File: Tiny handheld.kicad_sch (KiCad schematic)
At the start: 38 parts, among them J1 Conn_01x04_Female, J2 Conn_01x04_Female, J3 TYPE-C-31-M-12, U1 ATtiny85-20P, U2 ATtiny85-20M, U3 EEPROM-I2CEIAJ

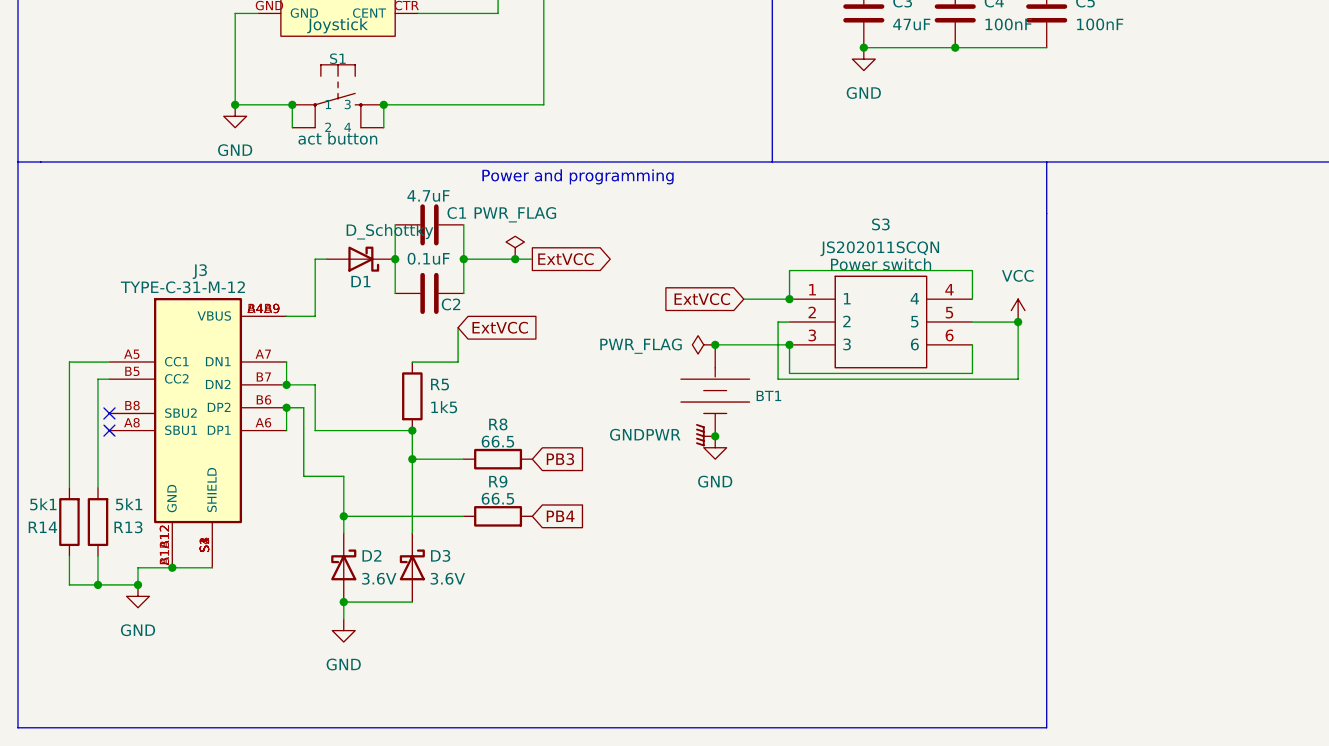
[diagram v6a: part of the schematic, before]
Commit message: added different switch in schematic
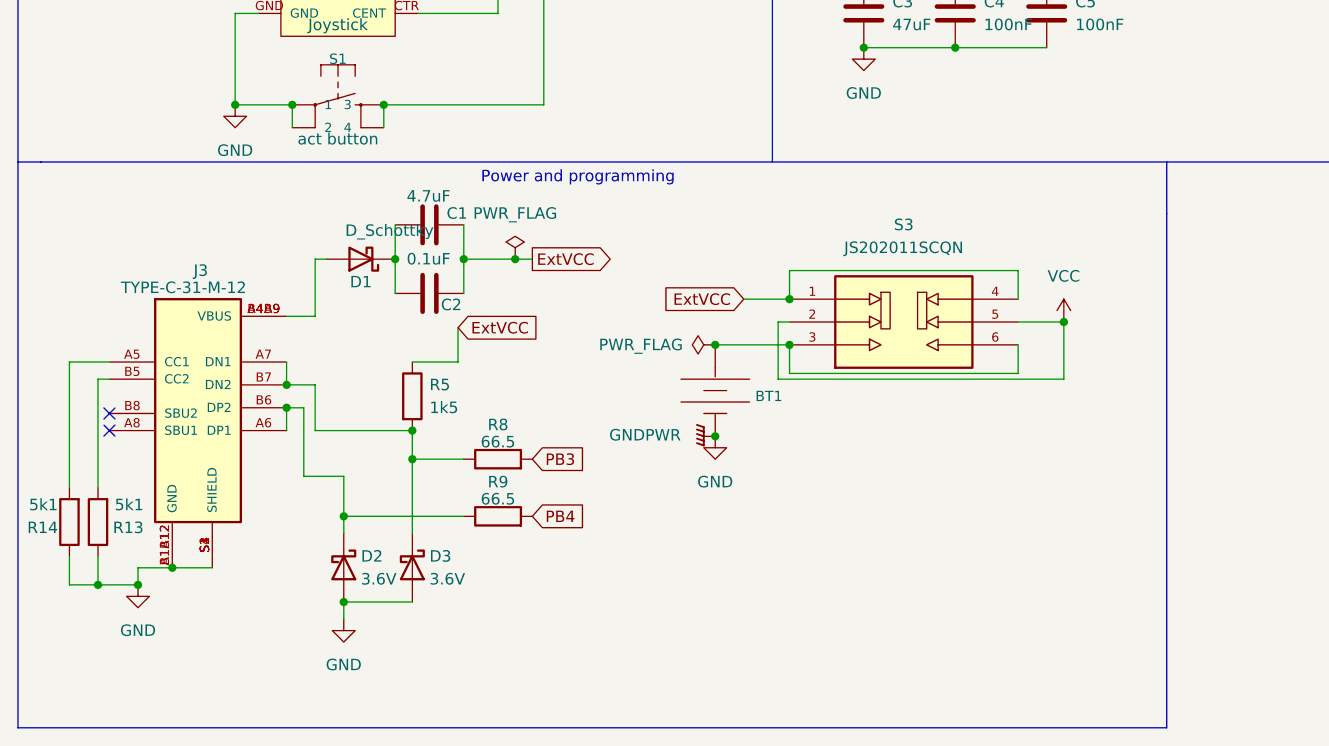
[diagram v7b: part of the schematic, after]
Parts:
- removed S3: JS202011SCQN, SmacSYs:JS202011SCQN, symbol SamacSys_Parts:JS202011SCQN
- added S3: JS202011SCQN, SnapEDA Library:SW_JS202011SCQN, symbol JS202011SCQN:JS202011SCQN
- U3: footprint Package_SO:SOIC-8-1EP_3.9x4.9mm_P1.27mm_EP2.41x3.81mm -> Package_SO:SOIC-8_3.9x4.9mm_P1.27mm
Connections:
- net ExtVCC: now also S3.1, S3.4
- net VCC: now also S3.2, S3.5
- net at BT1.+: now also S3.3, S3.6
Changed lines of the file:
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@@
   (junction (at 249.555 27.305) (diameter 0) (color 0 0 0 0)
   )
+  (junction (at 248.285 29.845) (diameter 0) (color 0 0 0 0)
+  )
+  (junction (at 132.715 54.61) (diameter 0) (color 0 0 0 0)
+  )
+  (junction (at 71.12 45.085) (diameter 0) (color 0 0 0 0)
+  )
+  (junction (at 71.12 29.845) (diameter 0) (color 0 0 0 0)
+  )
+  (junction (at 56.515 119.38) (diameter 0) (color 0 0 0 0)
+  )
   (junction (at 98.425 104.775) (diameter 0) (color 0 0 0 0)
   )
-  (junction (at 248.285 29.845) (diameter 0) (color 0 0 0 0)
-  )
-  (junction (at 132.715 54.61) (diameter 0) (color 0 0 0 0)
-  )
-  (junction (at 71.12 45.085) (diameter 0) (color 0 0 0 0)
-  )
-  (junction (at 71.12 29.845) (diameter 0) (color 0 0 0 0)
-  )
-  (junction (at 56.515 119.38) (diameter 0) (color 0 0 0 0)
-  )
   (junction (at 106.68 76.835) (diameter 0) (color 0 0 0 0)
   )
@@
   (junction (at 164.465 32.385) (diameter 0) (color 0 0 0 0)
   )
+  (junction (at 128.905 107.315) (diameter 0) (color 0 0 0 0)
+  )
   (junction (at 160.655 49.53) (diameter 0) (color 0 0 0 0)
   )
@@
   (junction (at 90.17 120.015) (diameter 0) (color 0 0 0 0)
   )
-  (junction (at 123.825 107.315) (diameter 0) (color 0 0 0 0)
+  (junction (at 98.425 109.855) (diameter 0) (color 0 0 0 0)
   )
   (junction (at 53.34 50.165) (diameter 0) (color 0 0 0 0)
@@
   )
   (junction (at 132.715 49.53) (diameter 0) (color 0 0 0 0)
-  )
-  (junction (at 98.425 109.855) (diameter 0) (color 0 0 0 0)
   )
   (no_connect (at 22.86 117.475))
@@
     (stroke (width 0) (type default) (color 0 0 0 0))
   )
-  (wire (pts (xy 118.745 109.855) (xy 118.745 113.03))
+  (wire (pts (xy 123.825 109.855) (xy 123.825 113.03))
     (stroke (width 0) (type default) (color 0 0 0 0))
   )
@@
     (stroke (width 0) (type default) (color 0 0 0 0))
   )
-  (polyline (pts (xy 127 89.535) (xy 127 95.25))
+  (polyline (pts (xy 140.335 89.535) (xy 140.335 95.25))
     (stroke (width 0) (type default) (color 0 0 0 0))
   )
@@
     (stroke (width 0) (type default) (color 0 0 0 0))
   )
-  (wire (pts (xy 118.745 107.315) (xy 123.825 107.315))
+  (wire (pts (xy 123.825 107.315) (xy 128.905 107.315))
     (stroke (width 0) (type default) (color 0 0 0 0))
   )
@@
     (stroke (width 0) (type default) (color 0 0 0 0))
   )
-  (wire (pts (xy 123.825 107.315) (xy 123.825 113.665))
+  (wire (pts (xy 128.905 107.315) (xy 128.905 113.665))
     (stroke (width 0) (type default) (color 0 0 0 0))
   )
@@
     (stroke (width 0) (type default) (color 0 0 0 0))
   )
-  (wire (pts (xy 118.745 113.03) (xy 98.425 113.03))
+  (wire (pts (xy 123.825 113.03) (xy 98.425 113.03))
     (stroke (width 0) (type default) (color 0 0 0 0))
   )
@@
     (stroke (width 0) (type default) (color 0 0 0 0))
   )
-  (wire (pts (xy 118.745 101.6) (xy 118.745 104.775))
+  (wire (pts (xy 123.825 101.6) (xy 123.825 104.775))
     (stroke (width 0) (type default) (color 0 0 0 0))
   )
@@
     (stroke (width 0) (type default) (color 0 0 0 0))
   )
-  (wire (pts (xy 123.825 113.665) (xy 97.155 113.665))
+  (wire (pts (xy 128.905 113.665) (xy 97.155 113.665))
     (stroke (width 0) (type default) (color 0 0 0 0))
   )
@@
     (stroke (width 0) (type default) (color 0 0 0 0))
   )
-  (polyline (pts (xy 127 95.25) (xy 127 152.4))
+  (polyline (pts (xy 140.335 95.25) (xy 140.335 152.4))
     (stroke (width 0) (type default) (color 0 0 0 0))
   )
@@
     (stroke (width 0) (type default) (color 0 0 0 0))
   )
-  (wire (pts (xy 98.425 101.6) (xy 118.745 101.6))
+  (wire (pts (xy 98.425 101.6) (xy 123.825 101.6))
     (stroke (width 0) (type default) (color 0 0 0 0))
   )
@@
     (stroke (width 0) (type default) (color 0 0 0 0))
   )
-  (polyline (pts (xy 127 152.4) (xy 12.7 152.4))
+  (polyline (pts (xy 140.335 152.4) (xy 12.7 152.4))
     (stroke (width 0) (type default) (color 0 0 0 0))
   )
@@
     )
     (pin "1")
+  )
+  (symbol (lib_id "JS202011SCQN:JS202011SCQN") (at 111.125 107.315 0) (unit 1)
+    (in_bom yes) (on_board yes) (fields_autoplaced)
+    (property "Reference" "S3" (id 0) (at 111.125 96.52 0))
+    (property "Value" "JS202011SCQN" (id 1) (at 111.125 99.06 0))
+    (property "Footprint" "SnapEDA Library:SW_JS202011SCQN" (id 2) (at 111.125 107.315 0)
+      (effects (font (size 1.27 1.27)) (justify left bottom) hide)
+    )
+    (property "Datasheet" "" (id 3) (at 111.125 107.315 0)
+      (effects (font (size 1.27 1.27)) (justify left bottom) hide)
+    )
+    (property "STANDARD" "Manufacturer Recommendations" (id 4) (at 111.125 107.315 0)
+      (effects (font (size 1.27 1.27)) (justify left bottom) hide)
+    )
+    (property "MANUFACTURER" "C&K" (id 5) (at 111.125 107.315 0)
+      (effects (font (size 1.27 1.27)) (justify left bottom) hide)
+    )
+    (property "MAXIMUM_PACKAGE_HEIGHT" "5.5 mm" (id 6) (at 111.125 107.315 0)
+      (effects (font (size 1.27 1.27)) (justify left bottom) hide)
+    )
+    (property "PARTREV" "26 May 22" (id 7) (at 111.125 107.315 0)
+      (effects (font (size 1.27 1.27)) (justify left bottom) hide)
+    )
+    (property "SNAPEDA_PN" "JS202011SCQN" (id 8) (at 111.125 107.315 0)
+      (effects (font (size 1.27 1.27)) (justify left bottom) hide)
+    )
+    (pin "1")
+    (pin "2")
+    (pin "3")
+    (pin "4")
+    (pin "5")
+    (pin "6")
   )
   (symbol (lib_id "Device:R") (at 56.515 115.57 0) (unit 1)
@@
     (pin "2")
   )
-  (symbol (lib_id "SamacSys_Parts:JS202011SCQN") (at 98.425 104.775 0) (unit 1)
-    (in_bom yes) (on_board yes)
-    (property "Reference" "S3" (id 0) (at 108.585 96.52 0))
-    (property "Value" "JS202011SCQN" (id 1) (at 108.585 99.06 0))
-    (property "Footprint" "SmacSYs:JS202011SCQN" (id 2) (at 114.935 102.235 0)
-      (effects (font (size 1.27 1.27)) (justify left) hide)
-    )
-    (property "Datasheet" "http://www.ckswitches.com/media/1422/js.pdf" (id 3) (at 114.935 104.775 0)
-      (effects (font (size 1.27 1.27)) (justify left) hide)
-    )
-    (property "Description" "Sub miniature slide switches" (id 4) (at 114.935 107.315 0)
-      (effects (font (size 1.27 1.27)) (justify left) hide)
-    )
-    (property "Height" "5.5" (id 5) (at 114.935 109.855 0)
-      (effects (font (size 1.27 1.27)) (justify left) hide)
-    )
-    (property "Mouser Part Number" "611-JS202011SCQN" (id 6) (at 114.935 112.395 0)
-      (effects (font (size 1.27 1.27)) (justify left) hide)
-    )
-    (property "Mouser Price/Stock" "https://www.mouser.co.uk/ProductDetail/CK/JS202011SCQN?qs=LgMIjt8LuD95JYWxZ7NvZA%3D%3D" (id 7) (at 114.935 114.935 0)
-      (effects (font (size 1.27 1.27)) (justify left) hide)
-    )
-    (property "Manufacturer_Name" "C & K COMPONENTS" (id 8) (at 114.935 117.475 0)
-      (effects (font (size 1.27 1.27)) (justify left) hide)
-    )
-    (property "Manufacturer_Part_Number" "JS202011SCQN" (id 9) (at 114.935 120.015 0)
-      (effects (font (size 1.27 1.27)) (justify left) hide)
-    )
-    (property "Purpose" "Power switch" (id 10) (at 108.585 100.965 0))
-    (pin "1")
-    (pin "2")
-    (pin "3")
-    (pin "4")
-    (pin "5")
-    (pin "6")
-  )
   (symbol (lib_id "Device:R") (at 36.83 26.035 0) (unit 1)
     (in_bom yes) (on_board yes) (fields_autoplaced)
@@
       (effects (font (size 1.143 1.143)))
     )
-    (property "Footprint" "Package_SO:SOIC-8-1EP_3.9x4.9mm_P1.27mm_EP2.41x3.81mm" (id 2) (at 145.415 44.45 0)
+    (property "Footprint" "Package_SO:SOIC-8_3.9x4.9mm_P1.27mm" (id 2) (at 145.415 44.45 0)
       (effects (font (size 0.508 0.508)) hide)
     )
@@
     (pin "1")
   )
-  (symbol (lib_id "power:VCC") (at 123.825 107.315 0) (unit 1)
-    (in_bom yes) (on_board yes) (fields_autoplaced)
-    (property "Reference" "#PWR0105" (id 0) (at 123.825 111.125 0)
-      (effects (font (size 1.27 1.27)) hide)
-    )
-    (property "Value" "VCC" (id 1) (at 123.825 102.235 0))
-    (property "Footprint" "" (id 2) (at 123.825 107.315 0)
-      (effects (font (size 1.27 1.27)) hide)
-    )
-    (property "Datasheet" "" (id 3) (at 123.825 107.315 0)
+  (symbol (lib_id "power:VCC") (at 128.905 107.315 0) (unit 1)
+    (in_bom yes) (on_board yes) (fields_autoplaced)
+    (property "Reference" "#PWR0105" (id 0) (at 128.905 111.125 0)
+      (effects (font (size 1.27 1.27)) hide)
+    )
+    (property "Value" "VCC" (id 1) (at 128.905 102.235 0))
+    (property "Footprint" "" (id 2) (at 128.905 107.315 0)
+      (effects (font (size 1.27 1.27)) hide)
+    )
+    (property "Datasheet" "" (id 3) (at 128.905 107.315 0)
       (effects (font (size 1.27 1.27)) hide)
     )
@@
       (reference "S2") (unit 1) (value "JOYSTICK_MINI") (footprint "Button_Switch_SMD:5 way button (joystick)")
     )
-    (path "/64db9791-933d-441b-9e19-5cc2be4320f8"
-      (reference "S3") (unit 1) (value "JS202011SCQN") (footprint "SmacSYs:JS202011SCQN")
+    (path "/1e667aba-2dfb-48f6-b4f2-13dfd0e0c95b"
+      (reference "S3") (unit 1) (value "JS202011SCQN") (footprint "SnapEDA Library:SW_JS202011SCQN")
     )
     (path "/c34a0e3d-eac9-4dbc-9c25-13abd3c3897d"
@@
     )
     (path "/8508e319-db8f-4af2-9619-bd74b1def42f"
-      (reference "U3") (unit 1) (value "EEPROM-I2CEIAJ") (footprint "Package_SO:SOIC-8-1EP_3.9x4.9mm_P1.27mm_EP2.41x3.81mm")
-    )
-  )
+      (reference "U3") (unit 1) (value "EEPROM-I2CEIAJ") (footprint "Package_SO:SOIC-8_3.9x4.9mm_P1.27mm")
+    )
+  )

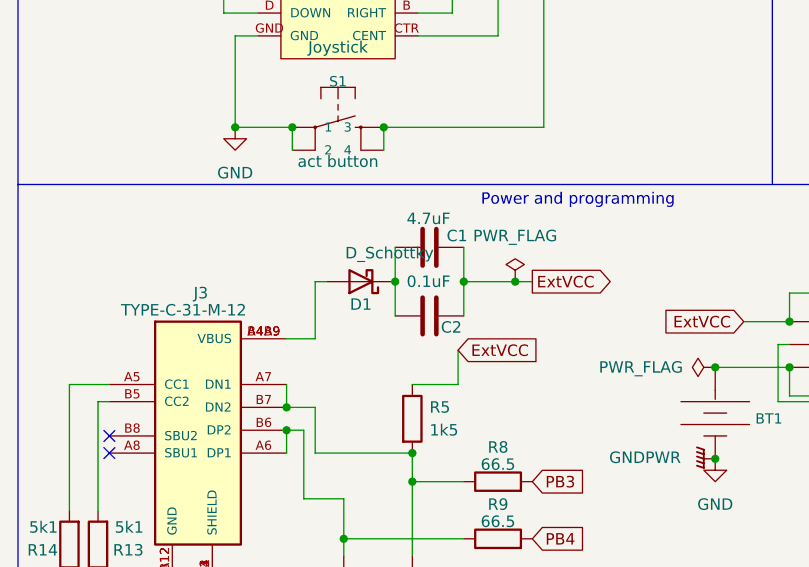
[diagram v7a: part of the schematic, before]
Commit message: fixed ERC error
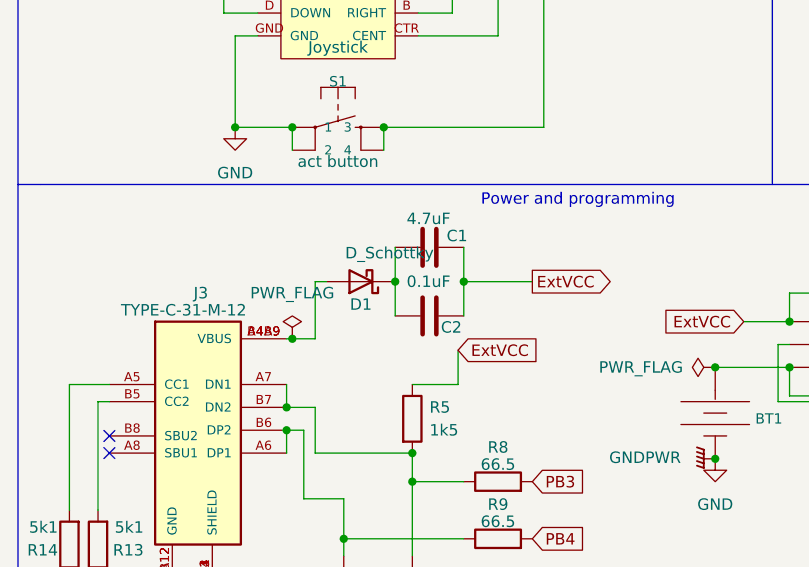
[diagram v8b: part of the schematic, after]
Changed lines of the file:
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@@
   (junction (at 130.175 35.56) (diameter 0) (color 0 0 0 0)
   )
+  (junction (at 43.18 106.68) (diameter 0) (color 0 0 0 0)
+  )
   (junction (at 21.59 136.525) (diameter 0) (color 0 0 0 0)
   )
@@
   )
   (junction (at 162.56 27.305) (diameter 0) (color 0 0 0 0)
-  )
-  (junction (at 67.945 100.33) (diameter 0) (color 0 0 0 0)
   )
   (junction (at 167.005 32.385) (diameter 0) (color 0 0 0 0)
@@
     (stroke (width 0) (type default) (color 0 0 0 0))
   )
-  (wire (pts (xy 62.23 100.33) (xy 67.945 100.33))
+  (wire (pts (xy 62.23 100.33) (xy 69.85 100.33))
     (stroke (width 0) (type default) (color 0 0 0 0))
   )
@@
     (stroke (width 0) (type default) (color 0 0 0 0))
   )
+  (wire (pts (xy 43.18 106.68) (xy 45.72 106.68))
+    (stroke (width 0) (type default) (color 0 0 0 0))
+  )
   (wire (pts (xy 58.42 67.945) (xy 57.15 67.945))
     (stroke (width 0) (type default) (color 0 0 0 0))
@@
     (stroke (width 0) (type default) (color 0 0 0 0))
   )
-  (wire (pts (xy 42.545 106.68) (xy 45.72 106.68))
+  (wire (pts (xy 42.545 106.68) (xy 43.18 106.68))
     (stroke (width 0) (type default) (color 0 0 0 0))
   )
@@
   )
   (polyline (pts (xy 195.58 13.335) (xy 195.58 89.535))
-    (stroke (width 0) (type default) (color 0 0 0 0))
-  )
-  (wire (pts (xy 67.945 100.33) (xy 69.85 100.33))
     (stroke (width 0) (type default) (color 0 0 0 0))
   )
@@
     (pin "2")
   )
-  (symbol (lib_id "power:PWR_FLAG") (at 67.945 100.33 0) (unit 1)
-    (in_bom yes) (on_board yes) (fields_autoplaced)
-    (property "Reference" "#FLG0101" (id 0) (at 67.945 98.425 0)
-      (effects (font (size 1.27 1.27)) hide)
-    )
-    (property "Value" "PWR_FLAG" (id 1) (at 67.945 95.25 0))
-    (property "Footprint" "" (id 2) (at 67.945 100.33 0)
-      (effects (font (size 1.27 1.27)) hide)
-    )
-    (property "Datasheet" "~" (id 3) (at 67.945 100.33 0)
-      (effects (font (size 1.27 1.27)) hide)
-    )
-    (pin "1")
-  )
   (symbol (lib_id "Device:D_Schottky") (at 48.895 134.62 270) (unit 1)
     (in_bom yes) (on_board yes)
@@
     )
     (property "Datasheet" "" (id 3) (at 36.83 22.225 0)
+      (effects (font (size 1.27 1.27)) hide)
+    )
+    (pin "1")
+  )
+  (symbol (lib_id "power:PWR_FLAG") (at 43.18 106.68 0) (unit 1)
+    (in_bom yes) (on_board yes) (fields_autoplaced)
+    (property "Reference" "#FLG0101" (id 0) (at 43.18 104.775 0)
+      (effects (font (size 1.27 1.27)) hide)
+    )
+    (property "Value" "PWR_FLAG" (id 1) (at 43.18 101.6 0))
+    (property "Footprint" "" (id 2) (at 43.18 106.68 0)
+      (effects (font (size 1.27 1.27)) hide)
+    )
+    (property "Datasheet" "~" (id 3) (at 43.18 106.68 0)
       (effects (font (size 1.27 1.27)) hide)
     )
@@
   )
   (symbol_instances
-    (path "/587111b3-1293-4783-b8d0-2a1d3dbe8587"
+    (path "/baec327b-179a-447f-ba38-182b88f29301"
       (reference "#FLG0101") (unit 1) (value "PWR_FLAG") (footprint "")
     )
